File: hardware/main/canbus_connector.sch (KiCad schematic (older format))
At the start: 4 parts, among them J601 RJ45, J602 RJ45

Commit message: Primeira versão do esquematico finalizada Falta DRC
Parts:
- gave numbers to parts that had none: 2
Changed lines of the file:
@@
 EESchema Schematic File Version 4
+LIBS:main-cache
 EELAYER 26 0
 EELAYER END
 $Descr A4 11693 8268
 encoding utf-8
-Sheet 5 7
+Sheet 5 8
 Title ""
 Date ""
@@
 CAN_H
 $Comp
-L Connector:RJ45_Shielded J?
+L Connector:RJ45_Shielded J2
 U 1 1 5C9C7D3B
 P 8800 3400
-F 0 "J?" H 9000 3950 50  0000 C CNN
+F 0 "J2" H 9000 3950 50  0000 C CNN
 F 1 "RJ45" H 8650 3950 50  0000 C CNN
 F 2 "KicadZeniteSolarLibrary18:RJ45_YH59_01" H 8800 3400 50  0001 C CNN
@@
 CAN_H
 $Comp
-L Connector:RJ45_Shielded J?
+L Connector:RJ45_Shielded J1
 U 1 1 5C9C7D58
 P 7250 3400
-F 0 "J?" H 7450 3950 50  0000 C CNN
+F 0 "J1" H 7450 3950 50  0000 C CNN
 F 1 "RJ45" H 7100 3950 50  0000 C CNN
 F 2 "KicadZeniteSolarLibrary18:RJ45_YH59_01" H 7250 3400 50  0001 C CNN
@@
 Connection ~ 7600 4500
 $Comp
-L power:GND #PWR?
+L power:GND #PWR0101
 U 1 1 5C9C7D70
 P 6050 4600
-F 0 "#PWR?" H 6050 4350 50  0001 C CNN
+F 0 "#PWR0101" H 6050 4350 50  0001 C CNN
 F 1 "GND" H 6100 4400 50  0000 C CNN
 F 2 "" H 6050 4600 50  0001 C CNN

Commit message: Abstração do esquemático modificada para separar as duas placas e mostrar a conexão entre elas na folha principal
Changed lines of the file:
@@
 EESchema Schematic File Version 4
 LIBS:main-cache
-EELAYER 26 0
+EELAYER 29 0
 EELAYER END
 $Descr A4 11693 8268
 encoding utf-8
-Sheet 5 8
+Sheet 5 9
 Title ""
 Date ""
@@
 U 1 1 5A01AFBA
 P 5450 3400
-F 0 "J602" H 5650 3950 50  0000 C CNN
+F 0 "J?" H 5650 3950 50  0000 C CNN
 F 1 "RJ45" H 5300 3950 50  0000 C CNN
 F 2 "KicadZeniteSolarLibrary18:RJ45_YH59_01" H 5450 3400 50  0001 C CNN
@@
 U 1 1 5BE6C2F7
 P 3900 3400
-F 0 "J601" H 4100 3950 50  0000 C CNN
+F 0 "J?" H 4100 3950 50  0000 C CNN
 F 1 "RJ45" H 3750 3950 50  0000 C CNN
 F 2 "KicadZeniteSolarLibrary18:RJ45_YH59_01" H 3900 3400 50  0001 C CNN
@@
 U 1 1 5BE6CF28
 P 2900 4600
-F 0 "#PWR0602" H 2900 4350 50  0001 C CNN
+F 0 "#PWR?" H 2900 4350 50  0001 C CNN
 F 1 "GND" H 2950 4400 50  0000 C CNN
 F 2 "" H 2900 4600 50  0001 C CNN
@@
 U 1 1 5BE70223
 P 2250 3800
-F 0 "#PWR0601" H 2250 3550 50  0001 C CNN
+F 0 "#PWR?" H 2250 3550 50  0001 C CNN
 F 1 "GND" H 2300 3600 50  0000 C CNN
 F 2 "" H 2250 3800 50  0001 C CNN
@@
 U 1 1 5C9C7D3B
 P 8800 3400
-F 0 "J2" H 9000 3950 50  0000 C CNN
+F 0 "J?" H 9000 3950 50  0000 C CNN
 F 1 "RJ45" H 8650 3950 50  0000 C CNN
 F 2 "KicadZeniteSolarLibrary18:RJ45_YH59_01" H 8800 3400 50  0001 C CNN
@@
 U 1 1 5C9C7D58
 P 7250 3400
-F 0 "J1" H 7450 3950 50  0000 C CNN
+F 0 "J?" H 7450 3950 50  0000 C CNN
 F 1 "RJ45" H 7100 3950 50  0000 C CNN
 F 2 "KicadZeniteSolarLibrary18:RJ45_YH59_01" H 7250 3400 50  0001 C CNN
@@
 U 1 1 5C9C7D70
 P 6050 4600
-F 0 "#PWR0101" H 6050 4350 50  0001 C CNN
+F 0 "#PWR?" H 6050 4350 50  0001 C CNN
 F 1 "GND" H 6100 4400 50  0000 C CNN
 F 2 "" H 6050 4600 50  0001 C CNN

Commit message: TO-DO List criada na folha principal
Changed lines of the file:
@@
 $Descr A4 11693 8268
 encoding utf-8
-Sheet 5 9
+Sheet 7 9
 Title ""
 Date ""
@@
 U 1 1 5A01AFBA
 P 5450 3400
-F 0 "J?" H 5650 3950 50  0000 C CNN
+AR Path="/5AAD16DD/5A01AFBA" Ref="J602"  Part="1"
+AR Path="/5CA4DC1F/5CA5A5C7/5A01AFBA" Ref="J702"  Part="1"
+F 0 "J702" H 5650 3950 50  0000 C CNN
 F 1 "RJ45" H 5300 3950 50  0000 C CNN
 F 2 "KicadZeniteSolarLibrary18:RJ45_YH59_01" H 5450 3400 50  0001 C CNN
@@
 U 1 1 5BE6C2F7
 P 3900 3400
-F 0 "J?" H 4100 3950 50  0000 C CNN
+AR Path="/5AAD16DD/5BE6C2F7" Ref="J601"  Part="1"
+AR Path="/5CA4DC1F/5CA5A5C7/5BE6C2F7" Ref="J701"  Part="1"
+F 0 "J701" H 4100 3950 50  0000 C CNN
 F 1 "RJ45" H 3750 3950 50  0000 C CNN
 F 2 "KicadZeniteSolarLibrary18:RJ45_YH59_01" H 3900 3400 50  0001 C CNN
@@
 U 1 1 5BE6CF28
 P 2900 4600
-F 0 "#PWR?" H 2900 4350 50  0001 C CNN
+AR Path="/5AAD16DD/5BE6CF28" Ref="#PWR0602"  Part="1"
+AR Path="/5CA4DC1F/5CA5A5C7/5BE6CF28" Ref="#PWR0137"  Part="1"
+F 0 "#PWR0137" H 2900 4350 50  0001 C CNN
 F 1 "GND" H 2950 4400 50  0000 C CNN
 F 2 "" H 2900 4600 50  0001 C CNN
@@
 U 1 1 5BE70223
 P 2250 3800
-F 0 "#PWR?" H 2250 3550 50  0001 C CNN
+AR Path="/5AAD16DD/5BE70223" Ref="#PWR0601"  Part="1"
+AR Path="/5CA4DC1F/5CA5A5C7/5BE70223" Ref="#PWR0138"  Part="1"
+F 0 "#PWR0138" H 2250 3550 50  0001 C CNN
 F 1 "GND" H 2300 3600 50  0000 C CNN
 F 2 "" H 2250 3800 50  0001 C CNN
@@
 U 1 1 5C9C7D3B
 P 8800 3400
-F 0 "J?" H 9000 3950 50  0000 C CNN
+AR Path="/5AAD16DD/5C9C7D3B" Ref="J2"  Part="1"
+AR Path="/5CA4DC1F/5CA5A5C7/5C9C7D3B" Ref="J704"  Part="1"
+F 0 "J704" H 9000 3950 50  0000 C CNN
 F 1 "RJ45" H 8650 3950 50  0000 C CNN
 F 2 "KicadZeniteSolarLibrary18:RJ45_YH59_01" H 8800 3400 50  0001 C CNN
@@
 U 1 1 5C9C7D58
 P 7250 3400
-F 0 "J?" H 7450 3950 50  0000 C CNN
+AR Path="/5AAD16DD/5C9C7D58" Ref="J1"  Part="1"
+AR Path="/5CA4DC1F/5CA5A5C7/5C9C7D58" Ref="J703"  Part="1"
+F 0 "J703" H 7450 3950 50  0000 C CNN
 F 1 "RJ45" H 7100 3950 50  0000 C CNN
 F 2 "KicadZeniteSolarLibrary18:RJ45_YH59_01" H 7250 3400 50  0001 C CNN
@@
 U 1 1 5C9C7D70
 P 6050 4600
-F 0 "#PWR?" H 6050 4350 50  0001 C CNN
+AR Path="/5AAD16DD/5C9C7D70" Ref="#PWR0101"  Part="1"
+AR Path="/5CA4DC1F/5CA5A5C7/5C9C7D70" Ref="#PWR0139"  Part="1"
+F 0 "#PWR0139" H 6050 4350 50  0001 C CNN
 F 1 "GND" H 6100 4400 50  0000 C CNN
 F 2 "" H 6050 4600 50  0001 C CNN

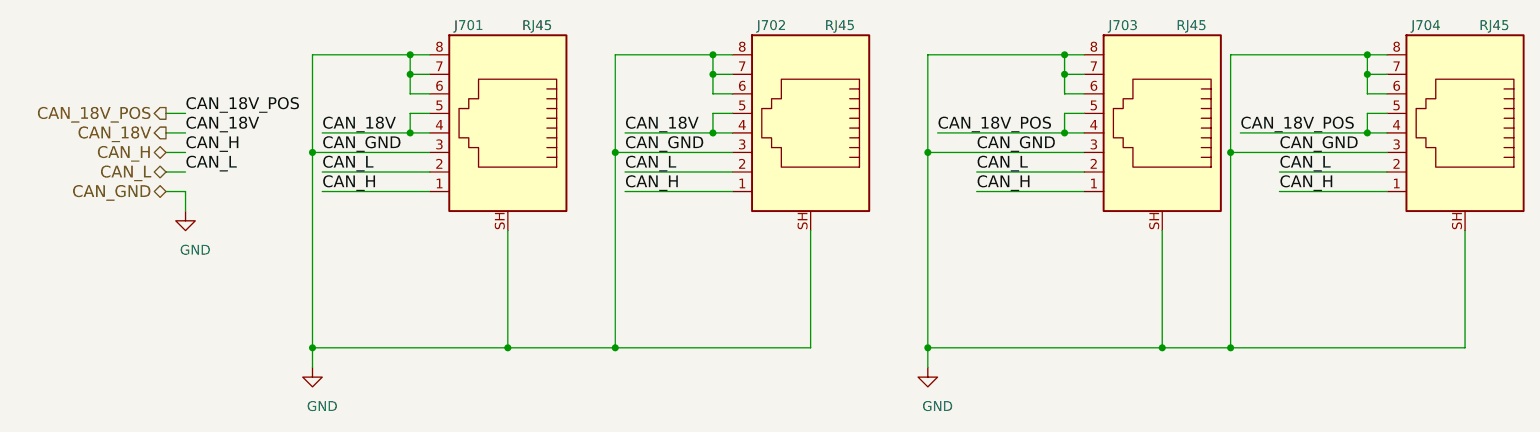
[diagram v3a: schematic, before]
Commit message: CAN CTRL_D / CAN_ON_OFF removidos.
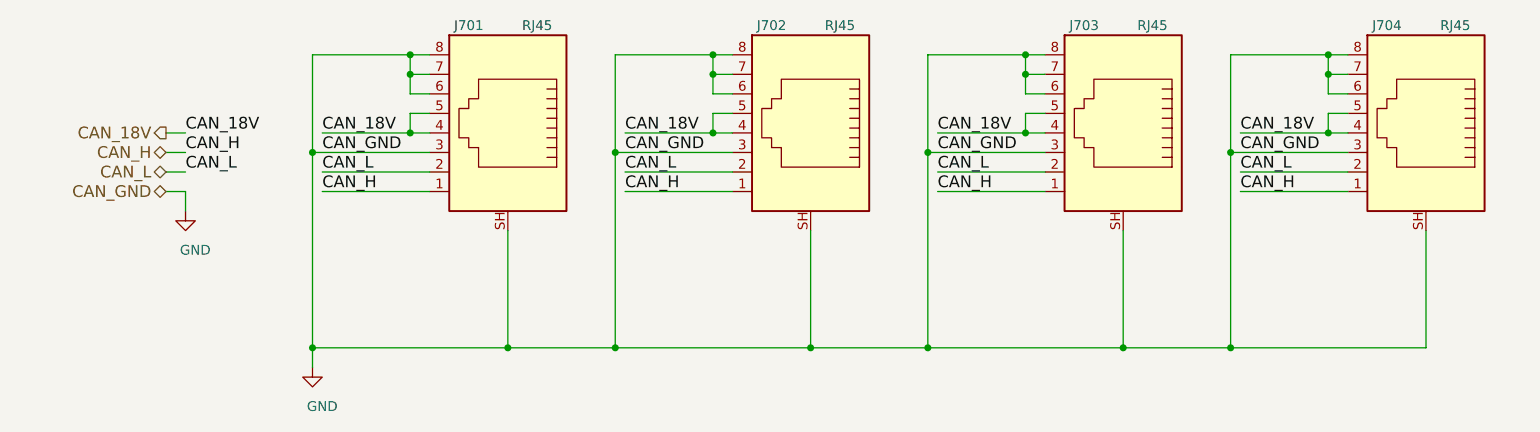
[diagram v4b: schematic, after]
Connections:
- net CAN_18V_POS is gone; now on net CAN_18V: J1.4, J1.5, J2.4, J2.5
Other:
- moved on the sheet: J703, J704
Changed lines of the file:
@@
 $Descr A4 11693 8268
 encoding utf-8
-Sheet 7 9
+Sheet 7 8
 Title ""
 Date ""
@@
 	4950 3200 4950 3100
 Connection ~ 4950 3100
-Wire Wire Line
-	8800 4500 8800 3900
-Wire Wire Line
-	7850 3600 8400 3600
-Wire Wire Line
-	8400 3700 7850 3700
-Text Label 7650 3400 0    60   ~ 0
-CAN_18V_POS
-Text Label 7850 3500 0    60   ~ 0
-CAN_GND
-Text Label 7850 3600 0    60   ~ 0
-CAN_L
-Text Label 7850 3700 0    60   ~ 0
-CAN_H
+Connection ~ 6050 4500
+Wire Wire Line
+	6050 3500 6050 4500
+Wire Wire Line
+	6050 3500 6650 3500
+Wire Wire Line
+	6550 3400 6650 3400
+Wire Wire Line
+	6550 3300 6550 3400
+Wire Wire Line
+	6650 3300 6550 3300
+Wire Wire Line
+	6650 3200 6550 3200
+Wire Wire Line
+	6550 3000 6050 3000
+Wire Wire Line
+	6550 3200 6550 3100
+Wire Wire Line
+	6550 3100 6550 3000
+Connection ~ 6550 3100
+Wire Wire Line
+	6650 3100 6550 3100
+Connection ~ 6050 3500
+Wire Wire Line
+	6050 3000 6050 3500
+Connection ~ 6550 3000
+Wire Wire Line
+	6650 3000 6550 3000
+$Comp
+L Connector:RJ45_Shielded J1
+U 1 1 5C9C7D58
+P 7050 3400
+AR Path="/5AAD16DD/5C9C7D58" Ref="J1"  Part="1"
+AR Path="/5CA4DC1F/5CA5A5C7/5C9C7D58" Ref="J703"  Part="1"
+F 0 "J703" H 7250 3950 50  0000 C CNN
+F 1 "RJ45" H 6900 3950 50  0000 C CNN
+F 2 "KicadZeniteSolarLibrary18:RJ45_YH59_01" H 7050 3400 50  0001 C CNN
+F 3 "" H 7050 3400 50  0001 C CNN
+	1    7050 3400
+	-1   0    0    -1
+$EndComp
+Text Label 6100 3700 0    60   ~ 0
+CAN_H
+Text Label 6100 3600 0    60   ~ 0
+CAN_L
+Text Label 6100 3500 0    60   ~ 0
+CAN_GND
+Wire Wire Line
+	6650 3700 6100 3700
+Wire Wire Line
+	6100 3600 6650 3600
+Wire Wire Line
+	7050 4500 7600 4500
+Wire Wire Line
+	6050 4500 7050 4500
+Connection ~ 7050 4500
+Wire Wire Line
+	7050 4500 7050 3900
+Wire Wire Line
+	7600 3500 7600 4500
+Wire Wire Line
+	7600 3500 8200 3500
+Wire Wire Line
+	8100 3400 8200 3400
+Wire Wire Line
+	8100 3300 8100 3400
+Wire Wire Line
+	8200 3300 8100 3300
+Wire Wire Line
+	8200 3200 8100 3200
+Wire Wire Line
+	8100 3000 7600 3000
+Wire Wire Line
+	8100 3200 8100 3100
+Wire Wire Line
+	8100 3100 8100 3000
+Connection ~ 8100 3100
+Wire Wire Line
+	8200 3100 8100 3100
+Connection ~ 7600 4500
+Wire Wire Line
+	7600 4500 8600 4500
+Connection ~ 7600 3500
+Wire Wire Line
+	7600 3000 7600 3500
+Connection ~ 8100 3000
+Wire Wire Line
+	8200 3000 8100 3000
 $Comp
 L Connector:RJ45_Shielded J2
 U 1 1 5C9C7D3B
-P 8800 3400
+P 8600 3400
 AR Path="/5AAD16DD/5C9C7D3B" Ref="J2"  Part="1"
 AR Path="/5CA4DC1F/5CA5A5C7/5C9C7D3B" Ref="J704"  Part="1"
-F 0 "J704" H 9000 3950 50  0000 C CNN
-F 1 "RJ45" H 8650 3950 50  0000 C CNN
-F 2 "KicadZeniteSolarLibrary18:RJ45_YH59_01" H 8800 3400 50  0001 C CNN
-F 3 "" H 8800 3400 50  0001 C CNN
-	1    8800 3400
+F 0 "J704" H 8800 3950 50  0000 C CNN
+F 1 "RJ45" H 8450 3950 50  0000 C CNN
+F 2 "KicadZeniteSolarLibrary18:RJ45_YH59_01" H 8600 3400 50  0001 C CNN
+F 3 "" H 8600 3400 50  0001 C CNN
+	1    8600 3400
 	-1   0    0    -1
 $EndComp
-Wire Wire Line
-	8400 3000 8300 3000
-Wire Wire Line
-	7600 3000 7600 3500
-Wire Wire Line
-	7600 4500 8800 4500
-Wire Wire Line
-	8400 3100 8300 3100
-Wire Wire Line
-	8300 3100 8300 3000
-Connection ~ 8300 3000
-Wire Wire Line
-	8300 3000 7600 3000
-Wire Wire Line
-	8400 3200 8300 3200
-Wire Wire Line
-	8400 3300 8300 3300
-Wire Wire Line
-	8300 3300 8300 3400
-Connection ~ 8300 3400
-Wire Wire Line
-	8300 3400 8400 3400
-Wire Wire Line
-	7600 3500 8400 3500
-Connection ~ 7600 3500
-Wire Wire Line
-	7600 3500 7600 4500
-Wire Wire Line
-	7250 4500 7250 3900
-Wire Wire Line
-	6300 3600 6850 3600
-Wire Wire Line
-	6850 3700 6300 3700
+Text Label 7650 3700 0    60   ~ 0
+CAN_H
+Text Label 7650 3600 0    60   ~ 0
+CAN_L
+Text Label 7650 3500 0    60   ~ 0
+CAN_GND
+Wire Wire Line
+	8200 3700 7650 3700
+Wire Wire Line
+	7650 3600 8200 3600
+Wire Wire Line
+	8600 4500 8600 3900
 Text Label 6100 3400 0    60   ~ 0
-CAN_18V_POS
-Text Label 6300 3500 0    60   ~ 0
-CAN_GND
-Text Label 6300 3600 0    60   ~ 0
-CAN_L
-Text Label 6300 3700 0    60   ~ 0
-CAN_H
-$Comp
-L Connector:RJ45_Shielded J1
-U 1 1 5C9C7D58
-P 7250 3400
-AR Path="/5AAD16DD/5C9C7D58" Ref="J1"  Part="1"
-AR Path="/5CA4DC1F/5CA5A5C7/5C9C7D58" Ref="J703"  Part="1"
-F 0 "J703" H 7450 3950 50  0000 C CNN
-F 1 "RJ45" H 7100 3950 50  0000 C CNN
-F 2 "KicadZeniteSolarLibrary18:RJ45_YH59_01" H 7250 3400 50  0001 C CNN
-F 3 "" H 7250 3400 50  0001 C CNN
-	1    7250 3400
-	-1   0    0    -1
-$EndComp
-Wire Wire Line
-	6850 3000 6750 3000
-Wire Wire Line
-	6050 3000 6050 3500
-Wire Wire Line
-	6050 4500 7250 4500
-Wire Wire Line
-	6850 3100 6750 3100
-Wire Wire Line
-	6750 3100 6750 3000
-Connection ~ 6750 3000
-Wire Wire Line
-	6750 3000 6050 3000
-Wire Wire Line
-	6850 3200 6750 3200
-Wire Wire Line
-	6850 3300 6750 3300
-Wire Wire Line
-	6750 3300 6750 3400
-Connection ~ 6750 3400
-Wire Wire Line
-	6750 3400 6850 3400
-Wire Wire Line
-	6050 3500 6850 3500
-Connection ~ 6050 3500
-Wire Wire Line
-	6050 3500 6050 4500
-Wire Wire Line
-	7250 4500 7600 4500
-Connection ~ 7250 4500
-Connection ~ 7600 4500
-$Comp
-L power:GND #PWR0101
-U 1 1 5C9C7D70
-P 6050 4600
-AR Path="/5AAD16DD/5C9C7D70" Ref="#PWR0101"  Part="1"
-AR Path="/5CA4DC1F/5CA5A5C7/5C9C7D70" Ref="#PWR0139"  Part="1"
-F 0 "#PWR0139" H 6050 4350 50  0001 C CNN
-F 1 "GND" H 6100 4400 50  0000 C CNN
-F 2 "" H 6050 4600 50  0001 C CNN
-F 3 "" H 6050 4600 50  0001 C CNN
-	1    6050 4600
-	1    0    0    -1
-$EndComp
-Wire Wire Line
-	6050 4500 6050 4600
-Connection ~ 6050 4500
-Wire Wire Line
-	6750 3200 6750 3100
-Connection ~ 6750 3100
-Wire Wire Line
-	8300 3200 8300 3100
-Connection ~ 8300 3100
-Wire Wire Line
-	6100 3400 6750 3400
-Wire Wire Line
-	7650 3400 8300 3400
-Text HLabel 2150 3300 0    60   Output ~ 0
-CAN_18V_POS
-Text Label 2250 3300 0    60   ~ 0
-CAN_18V_POS
-Wire Wire Line
-	2150 3300 2250 3300
+CAN_18V
+Text Label 7650 3400 0    60   ~ 0
+CAN_18V
+Wire Wire Line
+	6100 3400 6550 3400
+Connection ~ 6550 3400
+Wire Wire Line
+	8100 3400 7650 3400
+Connection ~ 8100 3400
+Wire Wire Line
+	5450 4500 6050 4500
+Connection ~ 5450 4500
 $EndSCHEMATC

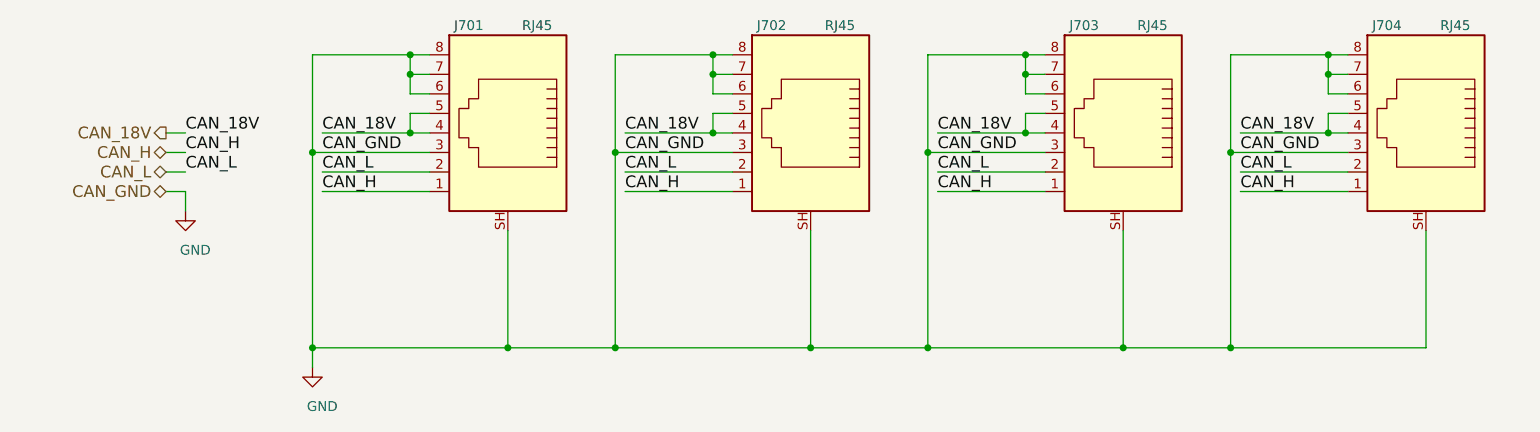
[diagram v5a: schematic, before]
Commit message: Esquematico primeira versão Erro de referencia dos componentes na PCB com os do Esquematico solucionados
Pontos de teste adicionados
Alimentar o analog com +12V
Adicionar Snubber para os reles
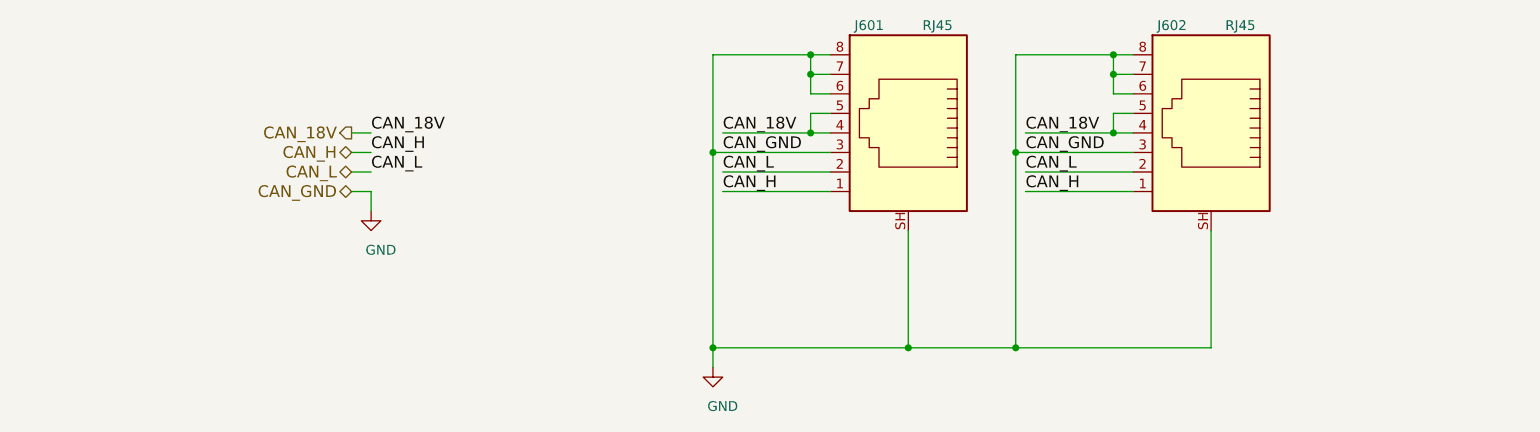
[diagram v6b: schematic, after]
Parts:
- removed J1, J2: RJ45, KicadZeniteSolarLibrary18:RJ45_YH59_01, symbol Connector:RJ45_Shielded
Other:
- moved on the sheet: J601, J602

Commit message: Footprints
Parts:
- added J1, J2: RJ45, KicadZeniteSolarLibrary18:RJ45_YH59_01, symbol Connector:RJ45_Shielded
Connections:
- net CAN_18V: now also J1.4, J1.5, J2.4, J2.5
- net CAN_H: now also J1.1, J2.1
- net CAN_L: now also J1.2, J2.2
- net GND: now also J1.3, J1.6, J1.7, J1.8, J1.SH, J2.3, J2.6, J2.7, J2.8, J2.SH
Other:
- moved on the sheet: J701, J702
